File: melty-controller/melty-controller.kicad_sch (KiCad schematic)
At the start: 39 parts, among them J1 Conn_01x02_Male, J2 soicbite, J3 esc_io, Q1 2N7002ET1G, U1 ESP32-PICO-D4, U2 MT2492, U3 MMA1200KEG

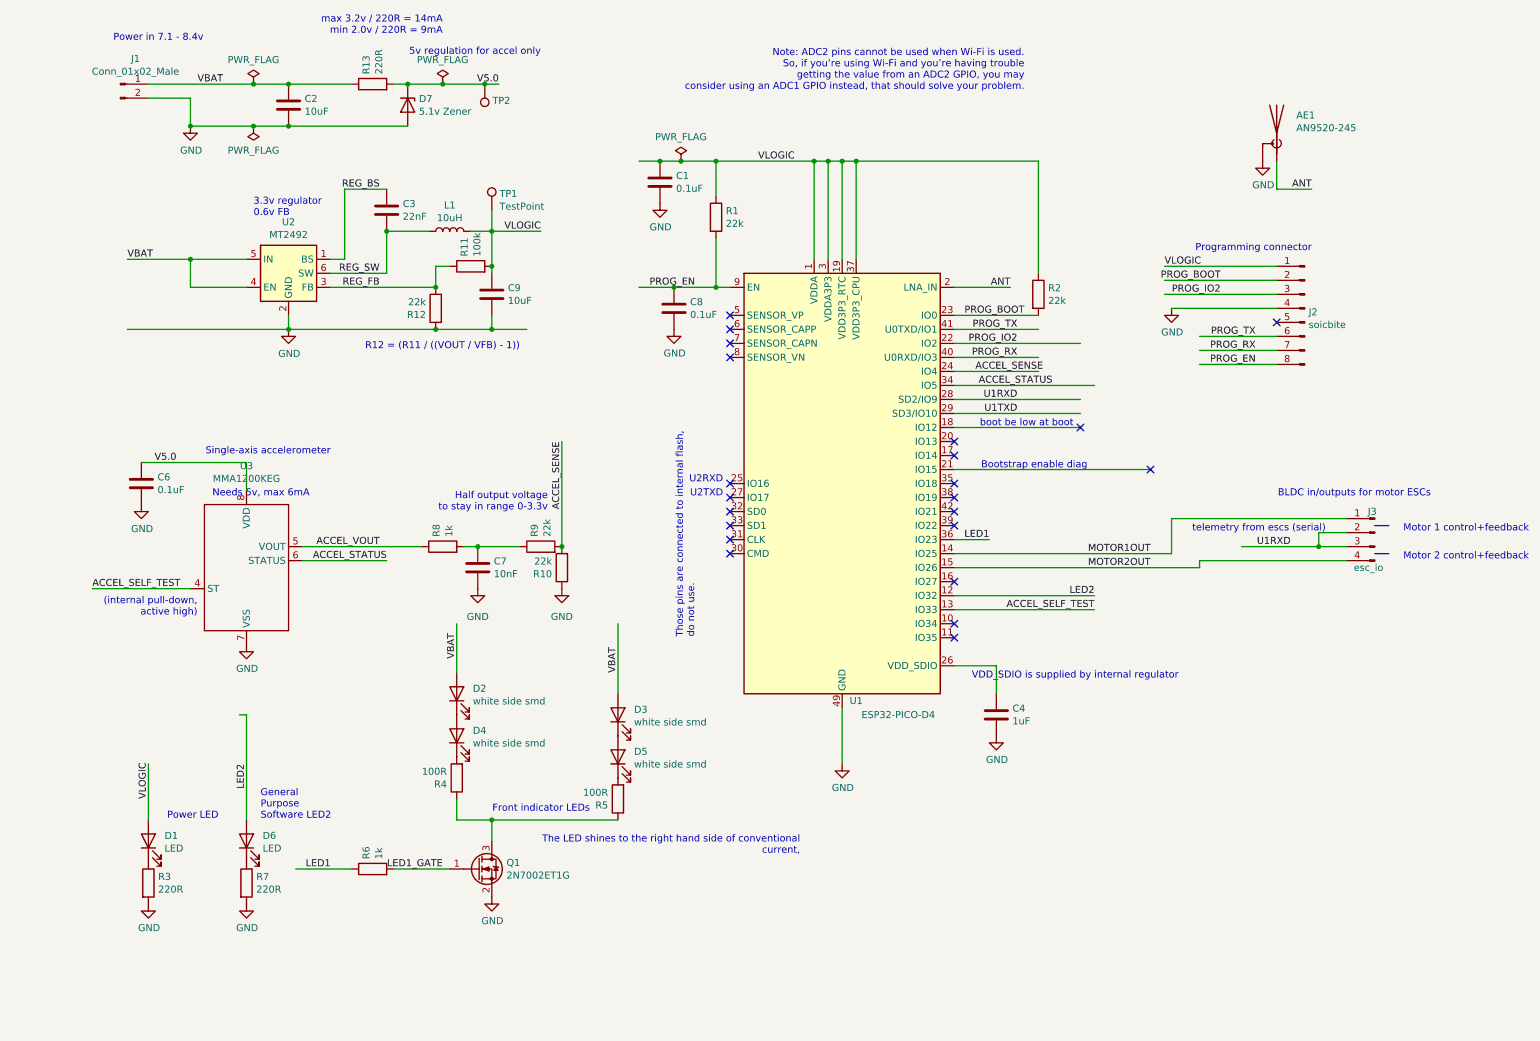
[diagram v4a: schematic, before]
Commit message: Use real regulator for 5.0 and tidy up schematic
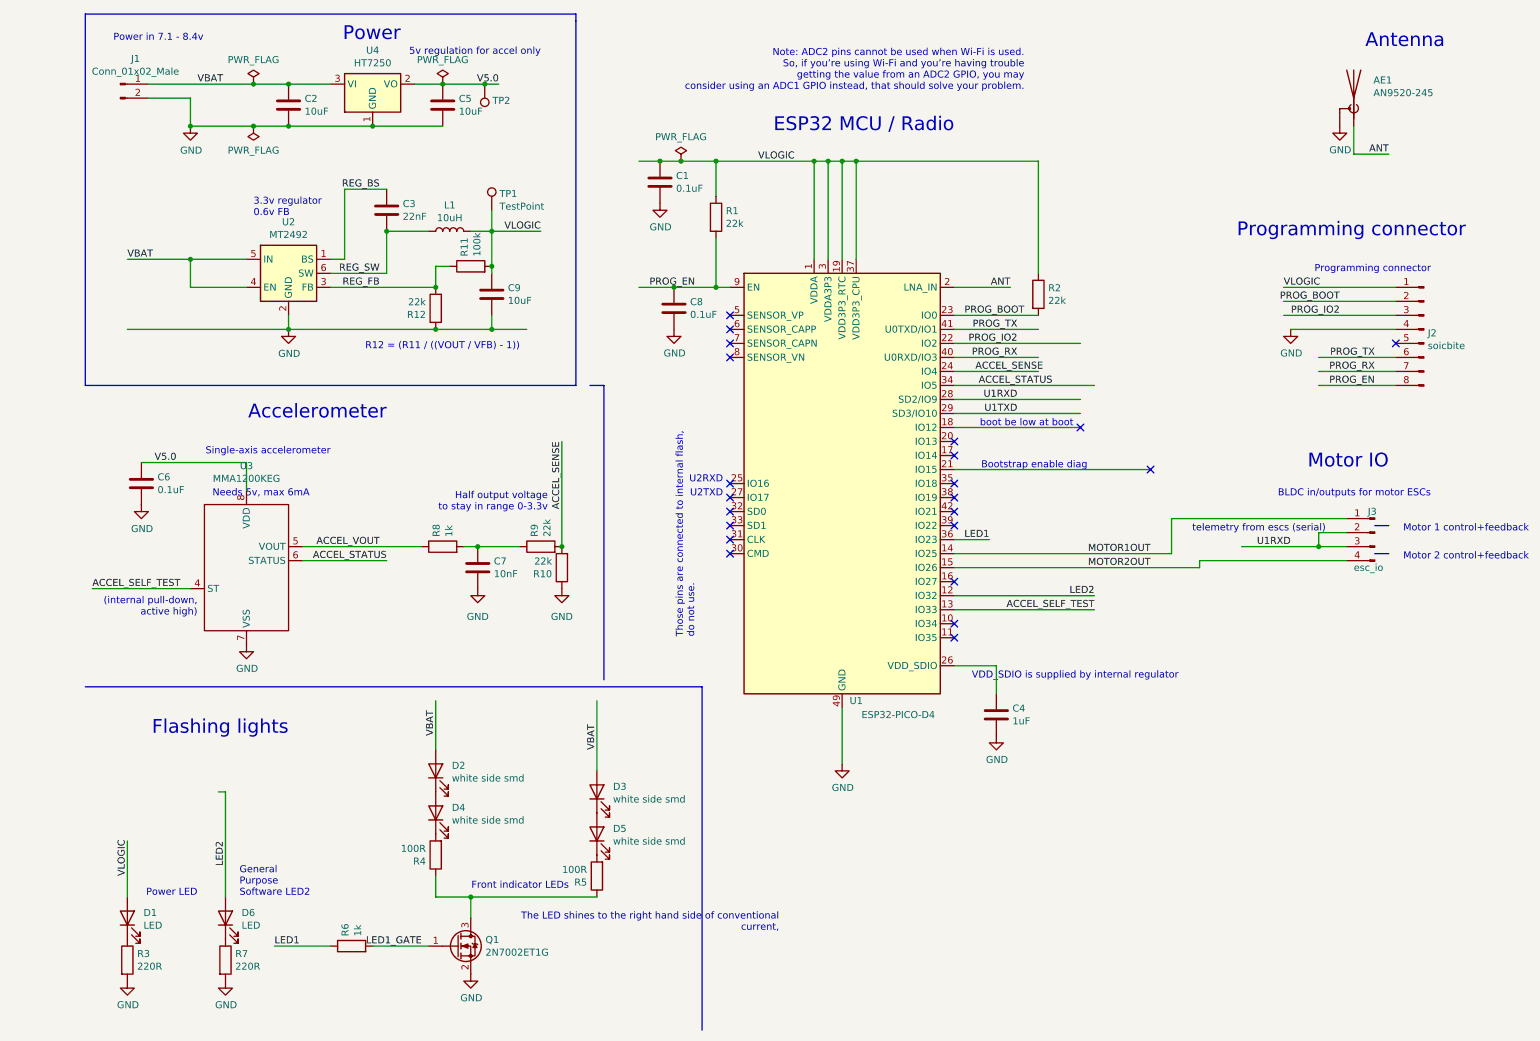
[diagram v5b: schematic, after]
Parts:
- removed D7: 5.1v Zener, Diode_SMD:D_SOD-323, symbol Device:D_Zener
- removed R13: 220R, Resistor_SMD:R_0603_1608Metric, symbol Device:R
- added C5: 10uF, Capacitor_SMD:C_0603_1608Metric, symbol Device:C
- added U4: HT7250, Package_TO_SOT_SMD:SOT-23, symbol melty1:HT7233
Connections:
- net GND: now also C5.2, U4.1 (GND)
- net V5.0: now also C5.1, U4.2 (VO)
- net VBAT: now also U4.3 (VI)
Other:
- note added: "Accelerometer"
- note added: "Antenna"
- note added: "ESP32 MCU / Radio"
- note added: "Flashing lights"
- note added: "Motor IO"
- note added: "Power"
- note removed: "max 3.2v / 220R = 14mA min 2.0v / 220R = 9mA"
- moved on the sheet: AE1, D1, D2, D3, D4, D5, D6, J2, Q1, R3, R4, R5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

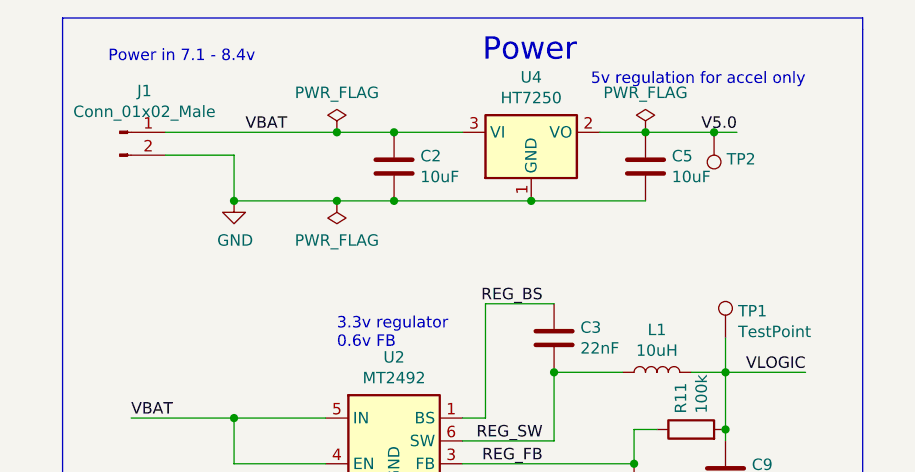
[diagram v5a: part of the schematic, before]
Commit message: Schematic updates; assign lcsc part numbers
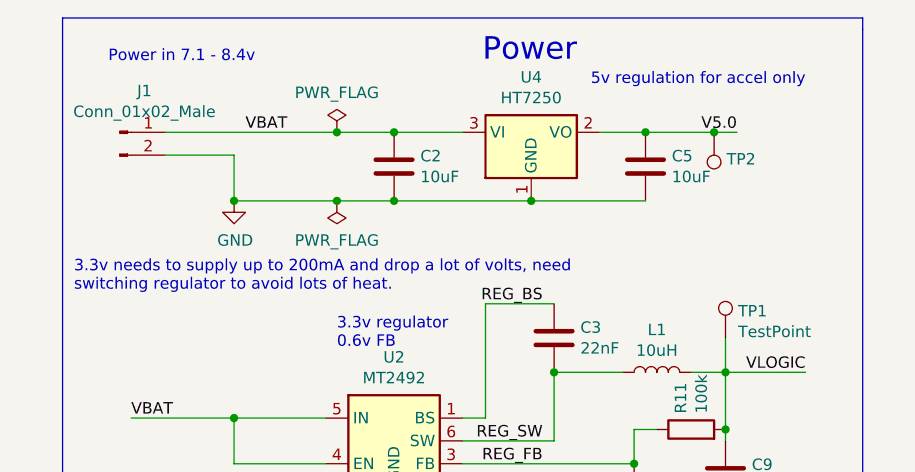
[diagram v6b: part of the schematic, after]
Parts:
- AE1: LCSC (none) -> C99665
- C1, C6, C8: LCSC C19702 -> C1591
- C3: LCSC (none) -> C21122
- C4: LCSC C19702 -> C15849
- C7: LCSC (none) -> C1589
- D1, D6: LCSC (none) -> C192318
- L1: LCSC (none) -> C250231
- R1, R10, R12, R2, R9: LCSC (none) -> C31850
- R11: LCSC (none) -> C25803
- R3, R7: LCSC (none) -> C22962
- R4, R5: LCSC (none) -> C22775
- R6, R8: LCSC (none) -> C21190
- U1: LCSC (none) -> C193707
- U2: LCSC (none) -> C89358
- U4: LCSC (none) -> C259602
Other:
- note added: "3.3v needs to supply up to 200mA and drop a lot of volts, need switching regulator to avoid lots of heat."
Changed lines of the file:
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@@
   (junction (at 153.67 40.64) (diameter 0) (color 0 0 0 0))
   (junction (at 237.49 110.49) (diameter 0) (color 0 0 0 0))
+  (no_connect (at 171.45 99.06))
+  (no_connect (at 171.45 116.84))
+  (no_connect (at 171.45 101.6))
+  (no_connect (at 251.46 73.66))
+  (no_connect (at 130.81 68.58))
+  (no_connect (at 171.45 124.46))
   (no_connect (at 171.45 91.44))
-  (no_connect (at 251.46 73.66))
+  (no_connect (at 130.81 109.22))
+  (no_connect (at 207.01 96.52))
+  (no_connect (at 130.81 73.66))
+  (no_connect (at 130.81 106.68))
+  (no_connect (at 171.45 127))
+  (no_connect (at 130.81 76.2))
+  (no_connect (at 171.45 104.14))
+  (no_connect (at 171.45 93.98))
+  (no_connect (at 130.81 71.12))
+  (no_connect (at 130.81 101.6))
+  (no_connect (at 171.45 106.68))
+  (no_connect (at 130.81 104.14))
+  (no_connect (at 130.81 111.76))
+  (no_connect (at 194.31 88.9))
   (no_connect (at 130.81 99.06))
-  (no_connect (at 171.45 93.98))
-  (no_connect (at 171.45 127))
-  (no_connect (at 130.81 106.68))
-  (no_connect (at 171.45 106.68))
-  (no_connect (at 130.81 101.6))
-  (no_connect (at 171.45 116.84))
-  (no_connect (at 194.31 88.9))
-  (no_connect (at 171.45 124.46))
-  (no_connect (at 130.81 104.14))
-  (no_connect (at 130.81 109.22))
-  (no_connect (at 130.81 111.76))
-  (no_connect (at 171.45 101.6))
-  (no_connect (at 171.45 104.14))
-  (no_connect (at 207.01 96.52))
-  (no_connect (at 130.81 76.2))
-  (no_connect (at 130.81 68.58))
-  (no_connect (at 171.45 99.06))
-  (no_connect (at 130.81 71.12))
-  (no_connect (at 130.81 73.66))
   (wire (pts (xy 15.24 118.11) (xy 33.02 118.11))
     (stroke (width 0) (type solid) (color 0 0 0 0))
@@
   (polyline (pts (xy 247.65 111.76) (xy 250.19 111.76))
     (stroke (width 0) (type solid) (color 0 0 0 0))
+  )
+  (text "3.3v needs to supply up to 200mA and drop a lot of volts, need\nswitching regulator to avoid lots of heat."
+    (at 15.24 44.45 0)
+    (effects (font (size 1.27 1.27)) (justify left bottom))
   )
   (text "Power in 7.1 - 8.4v" (at 19.05 19.05 0)
@@
     )
   )
-  (symbol (lib_id "malenki-nano-rescue:PWR_FLAG-power") (at 78.74 26.67 0) (unit 1)
-    (in_bom yes) (on_board yes)
-    (property "Reference" "#FLG0104" (id 0) (at 78.74 24.765 0)
-      (effects (font (size 1.27 1.27)) hide)
-    )
-    (property "Value" "PWR_FLAG" (id 1) (at 78.74 22.2758 0))
-    (property "Footprint" "" (id 2) (at 78.74 26.67 0)
-      (effects (font (size 1.27 1.27)) hide)
-    )
-    (property "Datasheet" "~" (id 3) (at 78.74 26.67 0)
-      (effects (font (size 1.27 1.27)) hide)
-    )
-  )
   (symbol (lib_id "malenki-nano-rescue:PWR_FLAG-power") (at 121.92 40.64 0) (unit 1)
     (in_bom yes) (on_board yes)
@@
       (effects (font (size 1.27 1.27)) hide)
     )
+    (property "LCSC" "C250231" (id 4) (at 80.01 53.34 0)
+      (effects (font (size 1.27 1.27)) hide)
+    )
   )
   (symbol (lib_id "power:GND") (at 21.59 189.23 0) (unit 1)
@@
       (effects (font (size 1.27 1.27)) hide)
     )
+    (property "LCSC" "C22962" (id 4) (at 21.59 185.42 0)
+      (effects (font (size 1.27 1.27)) hide)
+    )
   )
   (symbol (lib_id "Device:R") (at 39.37 185.42 0) (unit 1)
@@
       (effects (font (size 1.27 1.27)) hide)
     )
+    (property "LCSC" "C22962" (id 4) (at 39.37 185.42 0)
+      (effects (font (size 1.27 1.27)) hide)
+    )
   )
   (symbol (lib_id "Device:R") (at 62.23 182.88 90) (unit 1)
@@
       (effects (font (size 1.27 1.27)) hide)
     )
+    (property "LCSC" "C21190" (id 4) (at 62.23 182.88 0)
+      (effects (font (size 1.27 1.27)) hide)
+    )
   )
   (symbol (lib_id "Device:R") (at 77.47 67.31 180) (unit 1)
@@
       (effects (font (size 1.27 1.27)) hide)
     )
+    (property "LCSC" " C31850 " (id 4) (at 77.47 67.31 0)
+      (effects (font (size 1.27 1.27)) hide)
+    )
   )
   (symbol (lib_id "Device:R") (at 77.47 166.37 180) (unit 1)
@@
       (effects (font (size 1.27 1.27)) hide)
     )
+    (property "LCSC" "C22775" (id 4) (at 77.47 166.37 0)
+      (effects (font (size 1.27 1.27)) hide)
+    )
   )
   (symbol (lib_id "Device:R") (at 78.74 110.49 90) (unit 1)
@@
       (effects (font (size 1.27 1.27)) hide)
     )
+    (property "LCSC" "C21190" (id 4) (at 78.74 110.49 0)
+      (effects (font (size 1.27 1.27)) hide)
+    )
   )
   (symbol (lib_id "Device:R") (at 83.82 59.69 90) (unit 1)
@@
       (effects (font (size 1.27 1.27)) hide)
     )
+    (property "LCSC" "C25803" (id 4) (at 83.82 59.69 0)
+      (effects (font (size 1.27 1.27)) hide)
+    )
   )
   (symbol (lib_id "Device:R") (at 96.52 110.49 90) (unit 1)
@@
       (effects (font (size 1.27 1.27)) hide)
     )
+    (property "LCSC" " C31850 " (id 4) (at 96.52 110.49 0)
+      (effects (font (size 1.27 1.27)) hide)
+    )
   )
   (symbol (lib_id "Device:R") (at 100.33 114.3 180) (unit 1)
@@
       (effects (font (size 1.27 1.27)) hide)
     )
+    (property "LCSC" " C31850 " (id 4) (at 100.33 114.3 0)
+      (effects (font (size 1.27 1.27)) hide)
+    )
   )
   (symbol (lib_id "Device:R") (at 106.68 170.18 180) (unit 1)
@@
       (effects (font (size 1.27 1.27)) hide)
     )
+    (property "LCSC" "C22775" (id 4) (at 106.68 170.18 0)
+      (effects (font (size 1.27 1.27)) hide)
+    )
   )
   (symbol (lib_id "Device:R") (at 128.27 50.8 0) (unit 1)
@@
       (effects (font (size 1.27 1.27)) hide)
     )
+    (property "LCSC" " C31850 " (id 4) (at 128.27 50.8 0)
+      (effects (font (size 1.27 1.27)) hide)
+    )
   )
   (symbol (lib_id "Device:R") (at 186.69 64.77 0) (unit 1)
@@
     )
     (property "Datasheet" "~" (id 3) (at 186.69 64.77 0)
+      (effects (font (size 1.27 1.27)) hide)
+    )
+    (property "LCSC" " C31850 " (id 4) (at 186.69 64.77 0)
       (effects (font (size 1.27 1.27)) hide)
     )
@@
       (effects (font (size 1.27 1.27)) hide)
     )
+    (property "LCSC" "C192318" (id 4) (at 21.59 177.8 0)
+      (effects (font (size 1.27 1.27)) hide)
+    )
   )
   (symbol (lib_id "Device:LED") (at 39.37 177.8 90) (unit 1)
@@
       (effects (font (size 1.27 1.27)) hide)
     )
+    (property "LCSC" "C192318" (id 4) (at 39.37 177.8 0)
+      (effects (font (size 1.27 1.27)) hide)
+    )
   )
   (symbol (lib_id "Device:LED") (at 77.47 151.13 90) (unit 1)
@@
       (effects (font (size 1.27 1.27)) hide)
     )
-    (property "LCSC" "C19702" (id 5) (at 24.13 99.06 0)
+    (property "LCSC" "C1591" (id 5) (at 24.13 99.06 0)
       (effects (font (size 1.27 1.27)) hide)
     )
@@
       (effects (font (size 1.27 1.27)) hide)
     )
-    (property "LCSC" "" (id 5) (at 68.58 49.53 0)
+    (property "LCSC" "C21122" (id 5) (at 68.58 49.53 0)
       (effects (font (size 1.27 1.27)) hide)
     )
@@
       (effects (font (size 1.27 1.27)) hide)
     )
-    (property "LCSC" "" (id 5) (at 85.09 114.3 0)
+    (property "LCSC" "C1589" (id 5) (at 85.09 114.3 0)
       (effects (font (size 1.27 1.27)) hide)
     )
@@
       (effects (font (size 1.27 1.27)) hide)
     )
-    (property "LCSC" "C19702" (id 5) (at 118.11 44.45 0)
+    (property "LCSC" "C1591" (id 5) (at 118.11 44.45 0)
       (effects (font (size 1.27 1.27)) hide)
     )
@@
       (effects (font (size 1.27 1.27)) hide)
     )
-    (property "LCSC" "C19702" (id 5) (at 120.65 67.31 0)
+    (property "LCSC" "C1591" (id 5) (at 120.65 67.31 0)
       (effects (font (size 1.27 1.27)) hide)
     )
@@
       (effects (font (size 1.27 1.27)) hide)
     )
-    (property "LCSC" "C19702" (id 5) (at 179.07 140.97 0)
+    (property "LCSC" "C15849" (id 5) (at 179.07 140.97 0)
       (effects (font (size 1.27 1.27)) hide)
     )
@@
     )
     (property "Datasheet" "https://datasheet.lcsc.com/szlcsc/Rainsun-microwave-Tech-AN9520-245_C99665.pdf" (id 3) (at 246.38 24.765 0)
+      (effects (font (size 1.27 1.27)) hide)
+    )
+    (property "LCSC" "C99665" (id 4) (at 243.84 29.21 0)
       (effects (font (size 1.27 1.27)) hide)
     )
@@
     )
     (property "Datasheet" "https://datasheet.lcsc.com/szlcsc/1809191917_Holtek-Semicon-HT7233_C47970.pdf" (id 3) (at 66.04 22.86 0)
+      (effects (font (size 1.27 1.27)) hide)
+    )
+    (property "LCSC" "C259602" (id 4) (at 66.04 22.86 0)
       (effects (font (size 1.27 1.27)) hide)
     )
@@
       (effects (font (size 1.27 1.27)) hide)
     )
+    (property "LCSC" "C89358" (id 4) (at 50.8 60.96 0)
+      (effects (font (size 1.27 1.27)) hide)
+    )
   )
   (symbol (lib_id "melty1:MMA1200KEG") (at 43.18 118.11 0) (unit 1)
@@
       (effects (font (size 1.27 1.27)) hide)
     )
+    (property "LCSC" "C193707" (id 4) (at 151.13 99.06 0)
+      (effects (font (size 1.27 1.27)) hide)
+    )
   )
   (symbol_instances
@@
       (reference "#FLG0103") (unit 1)
     )
-    (path "/5cc5ef0f-3777-4492-bb7c-3cda39b204f0"
-      (reference "#FLG0104") (unit 1)
-    )
     (path "/983be544-9de7-4ac6-8757-1d47b7a21d70"
